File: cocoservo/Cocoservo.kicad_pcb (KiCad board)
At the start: 2 copper layers, 34 x 30 mm, 20 parts, among them U1 TSR1-2450

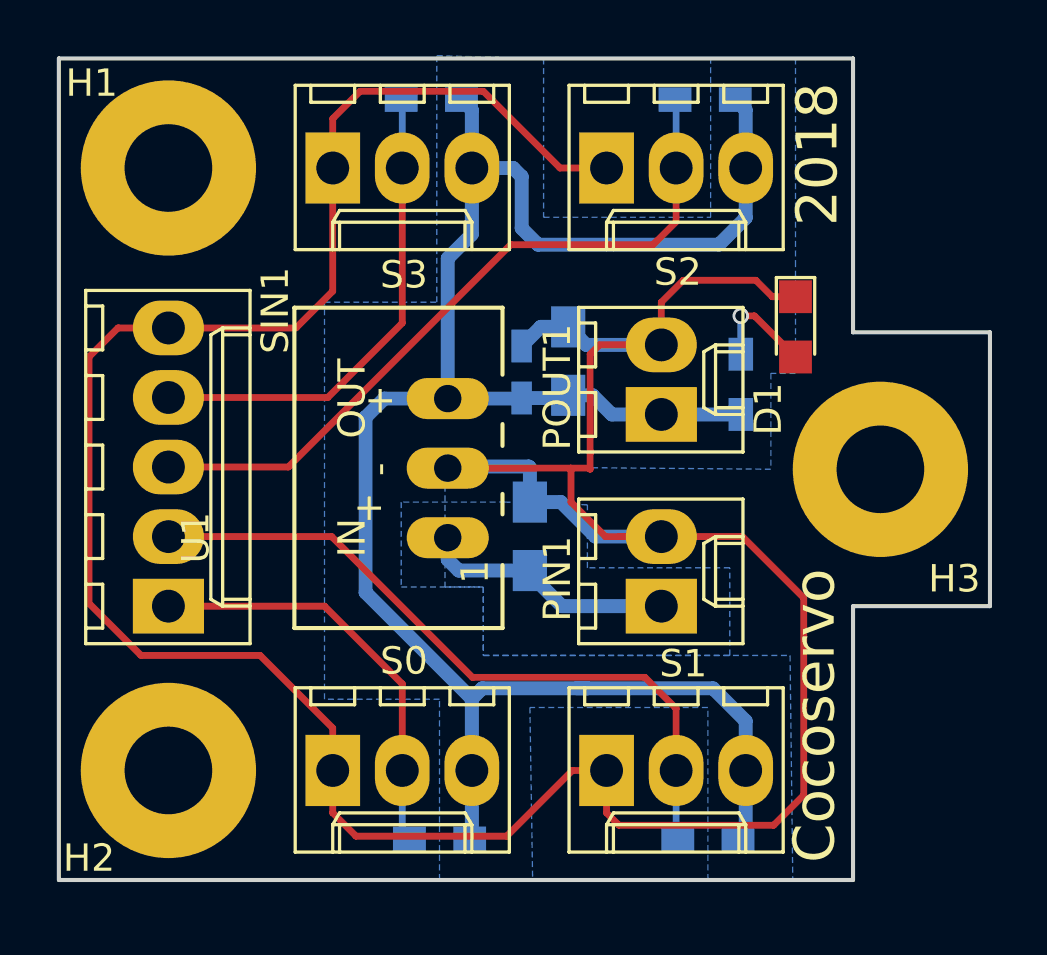
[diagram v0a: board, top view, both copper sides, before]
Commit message: ad 3d step files to cocoservo
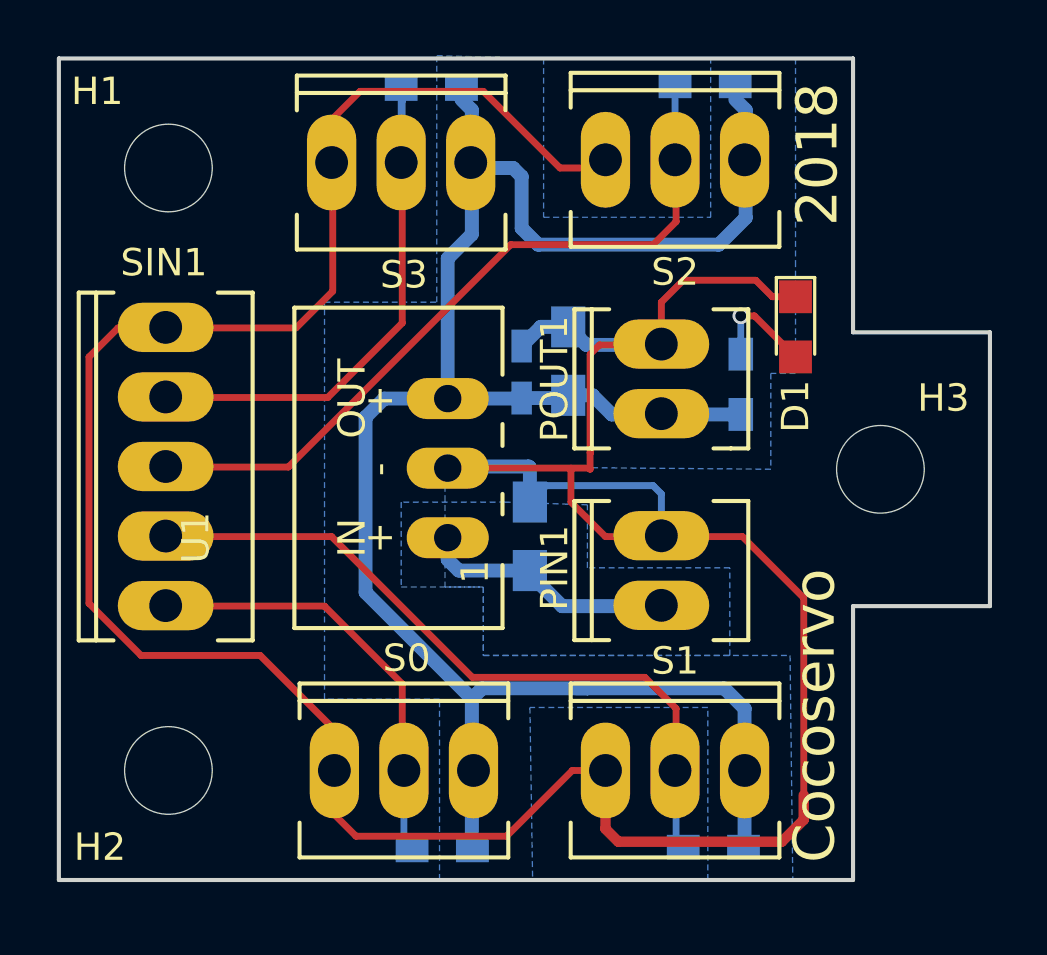
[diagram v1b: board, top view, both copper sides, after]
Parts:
- C1, C2: footprint Capacitors_SMD:C_0805_HandSoldering -> espitall:C_0805_HandSoldering
- C3: footprint Capacitors_SMD:C_0603_HandSoldering -> espitall:C_0603_HandSoldering
- D1: footprint LEDs:LED_0805 -> espitall:LED_0805
- H1, H2, H3: footprint Mounting_Holes:MountingHole_3.2mm_M3_Pad -> Mounting_Holes:MountingHole_3.2mm_M3
- PIN1, POUT1: footprint Connectors_Molex:Molex_KK-6410-02_02x2.54mm_Straight -> espitall:Socket_MOLEX-KK-RM2-54mm_Lock_2pin_straight
- R1, R2, R3, R4, R5: footprint Resistors_SMD:R_0603_HandSoldering -> espitall:R_0603_HandSoldering
- S0, S1, S2, S3: footprint Connectors_Molex:Molex_KK-6410-03_03x2.54mm_Straight -> espitall:Socket_MOLEX-KK-RM2-54mm_Lock_3pin_straight
- SIN1: footprint Connectors_Molex:Molex_KK-6410-05_05x2.54mm_Straight -> espitall:Socket_MOLEX-KK-RM2-54mm_Lock_5pin_straight
- moved SIN1 5.10 mm to (53.9, 64.9)
- moved S0 2.60 mm to (62.6, 76.0)
- moved S2 2.52 mm to (72.5, 53.7)
- moved S3 2.51 mm to (62.5, 53.8)
- moved S1 2.50 mm to (72.5, 76.0)
- moved PIN1 1.30 mm to (72.0, 68.7)
- moved POUT1 1.30 mm to (72.0, 61.7)
- moved R4 0.50 mm to (73.6, 51.0)
- moved R2 0.41 mm to (64.0, 78.9)
- moved R5 0.40 mm to (63.6, 51.1)
- moved R3 0.36 mm to (73.9, 78.8)
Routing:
- net +5P: track 75.4 -> 81.5 mm
- net GND: track 126.7 -> 131.1 mm
- net /servo_3_5v: track 17.8 -> 20.5 mm
